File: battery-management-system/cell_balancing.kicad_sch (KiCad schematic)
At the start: 0 parts

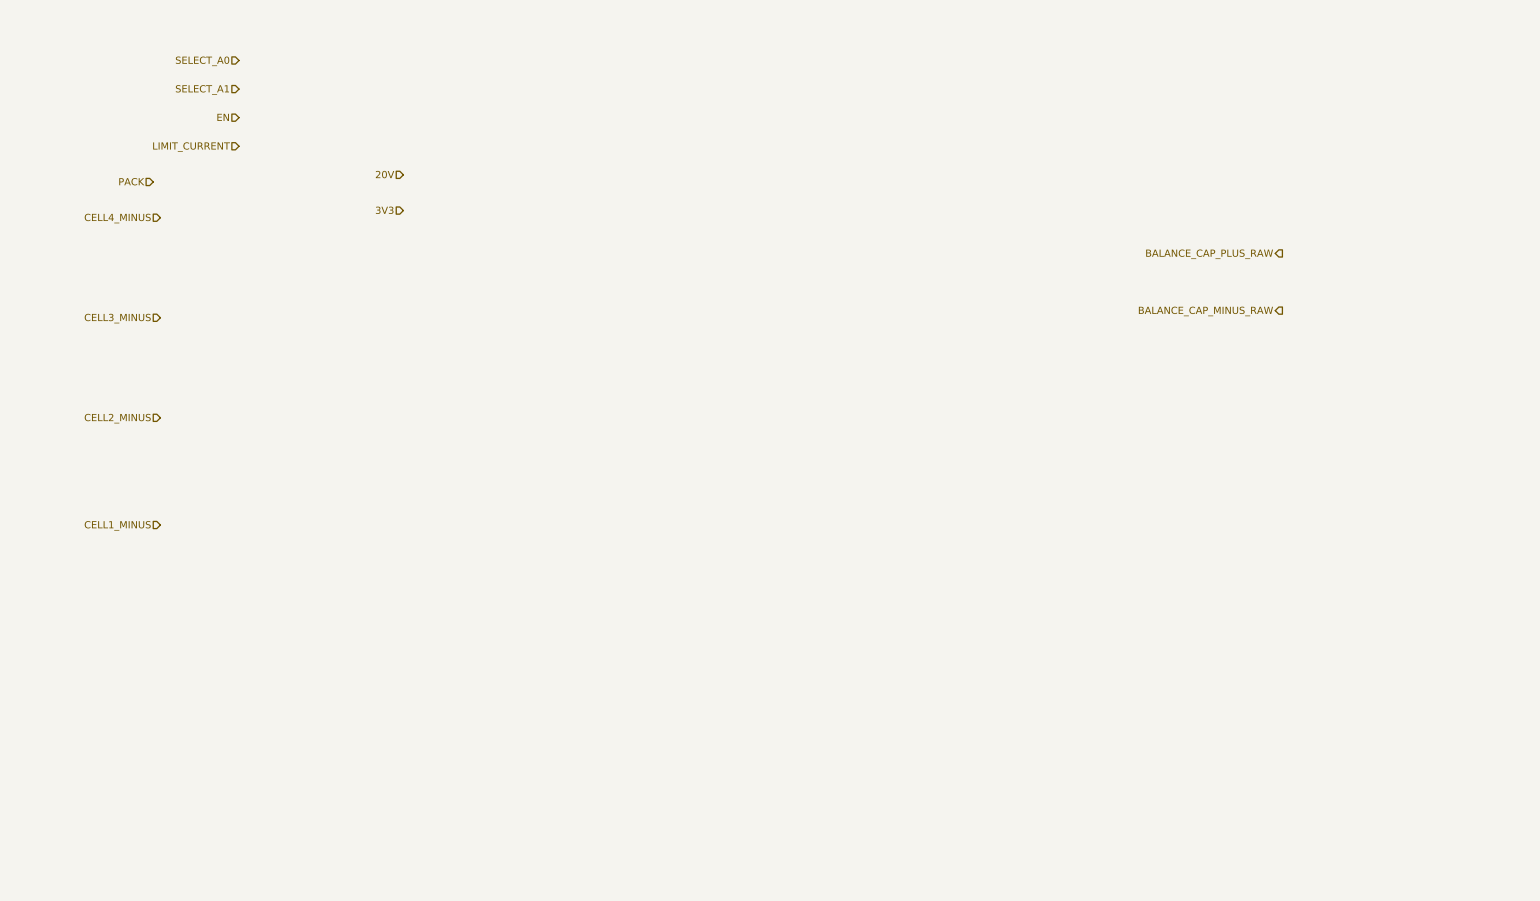
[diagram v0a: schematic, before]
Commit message: implement balancing
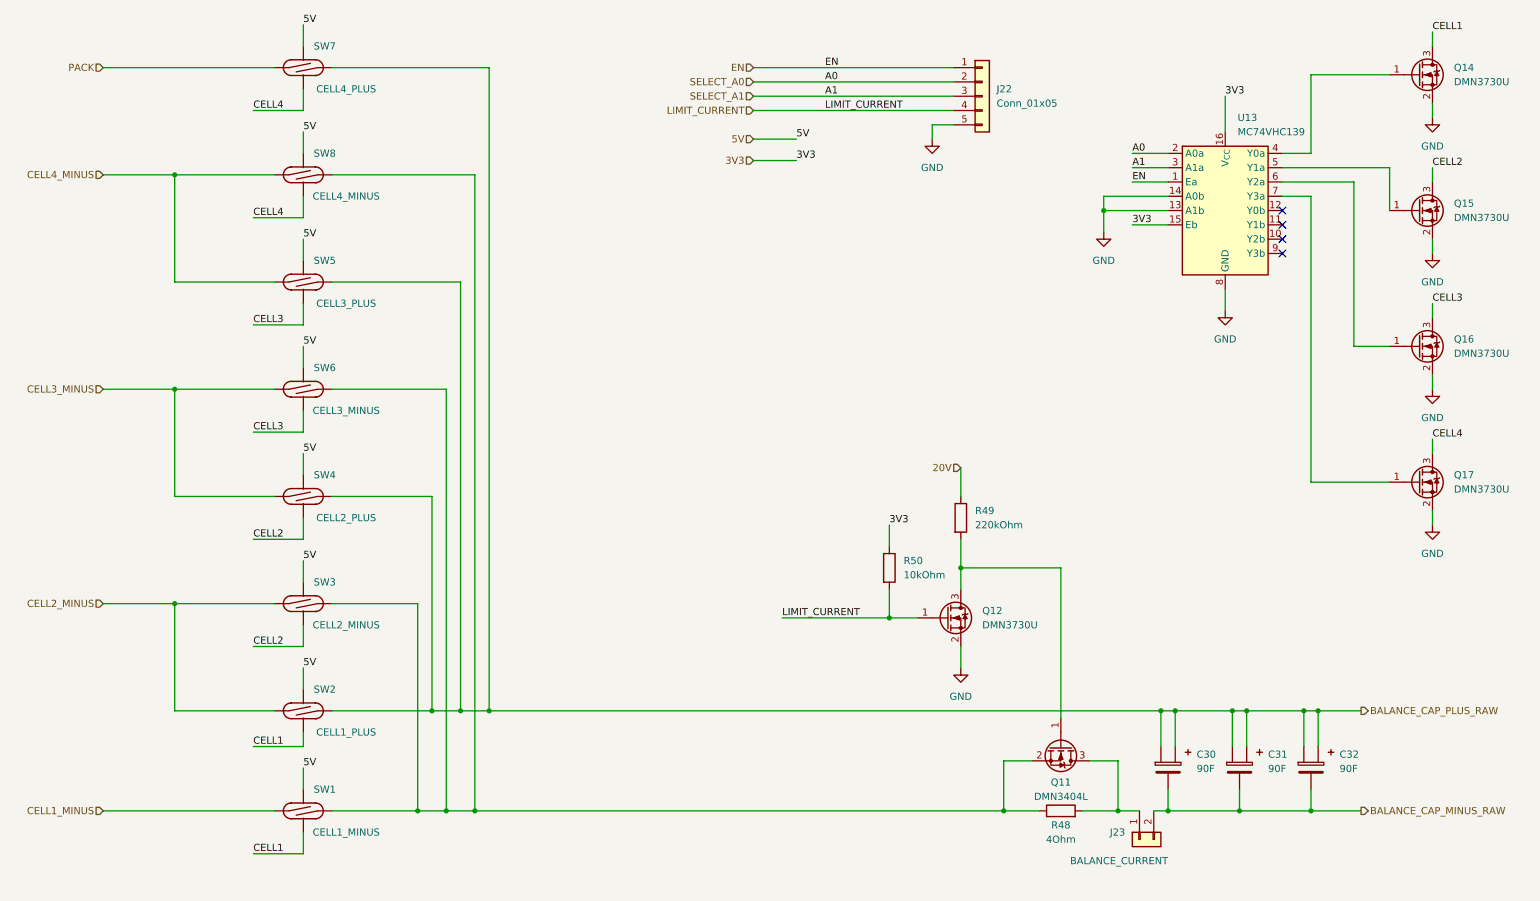
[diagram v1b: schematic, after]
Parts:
- added C30, C31, C32: 90F, benediktibk:vishay_super_cap_form_g, symbol benediktibk:C_90F_THT_4_2V
- added J22: Conn_01x05, benediktibk:PinHeader_1x05_P2.54mm_Vertical, symbol benediktibk:Conn_01x05
- added J23: BALANCE_CURRENT, benediktibk:PinHeader_1x02_P2.54mm_Vertical, symbol benediktibk:Conn_01x02
- added Q11: DMN3404L, benediktibk:SOT-23, symbol benediktibk:DMN3404L
- added Q12, Q14, Q15, Q16, Q17: DMN3730U, benediktibk:SOT-23, symbol benediktibk:DMN3730U
- added R48: 4Ohm, benediktibk:TO-263-resistor, symbol benediktibk:R_4Ohm_SMD_35W_1%
- added R49: 220kOhm, benediktibk:R_0603_1608Metric_Pad0.98x0.95mm_HandSolder, symbol benediktibk:R_220kOhm_SMD_0603_100mW_1%
- added R50: 10kOhm, benediktibk:R_0603_1608Metric_Pad0.98x0.95mm_HandSolder, symbol benediktibk:R_10kOhm_SMD_0603_100mW_1%
- added SW1: CELL1_MINUS, benediktibk:SIL05-1A72-BV669, symbol benediktibk:SIL05-1A72-BV669
- added SW2: CELL1_PLUS, benediktibk:SIL05-1A72-BV669, symbol benediktibk:SIL05-1A72-BV669
- added SW3: CELL2_MINUS, benediktibk:SIL05-1A72-BV669, symbol benediktibk:SIL05-1A72-BV669
- added SW4: CELL2_PLUS, benediktibk:SIL05-1A72-BV669, symbol benediktibk:SIL05-1A72-BV669
- added SW5: CELL3_PLUS, benediktibk:SIL05-1A72-BV669, symbol benediktibk:SIL05-1A72-BV669
- added SW6: CELL3_MINUS, benediktibk:SIL05-1A72-BV669, symbol benediktibk:SIL05-1A72-BV669
- added SW7: CELL4_PLUS, benediktibk:SIL05-1A72-BV669, symbol benediktibk:SIL05-1A72-BV669
- added SW8: CELL4_MINUS, benediktibk:SIL05-1A72-BV669, symbol benediktibk:SIL05-1A72-BV669
- added U13: MC74VHC139, benediktibk:TSSOP-16_4.4x5mm_P0.65mm, symbol benediktibk:MC74VHC139
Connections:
- net 20V: now also R49.1
- net 3V3: now also R50.1, U13.15 (Eb), U13.16 (V_{CC})
- net BALANCE_CAP_MINUS_RAW: now also C30.1, C31.1, C32.1, J23.2 (Pin_2)
- net BALANCE_CAP_PLUS_RAW: now also C30.2, C30.3, C31.2, C31.3, C32.2, C32.3, SW2.7 (+), SW4.7 (+), SW5.7 (+), SW7.7 (+)
- net CELL1_MINUS: now also SW1.1 (-)
- net CELL2_MINUS: now also SW2.1 (-), SW3.1 (-)
- net CELL3_MINUS: now also SW4.1 (-), SW6.1 (-)
- net CELL4_MINUS: now also SW5.1 (-), SW8.1 (-)
- net EN: now also J22.1 (Pin_1), U13.1 (Ea)
- net LIMIT_CURRENT: now also J22.4 (Pin_4), Q12.1 (G), R50.2
- net PACK: now also SW7.1 (-)
- net SELECT_A0: now also J22.2 (Pin_2), U13.2 (A0a)
- net SELECT_A1: now also J22.3 (Pin_3), U13.3 (A1a)
- new net: Q16.1 (G), U13.6 (Y2a)
- new net: Q14.1 (G), U13.4 (Y0a)
- new net: Q11.1 (G), Q12.3 (D), R49.2
- new net: Q11.2 (S), R48.1, SW1.7 (+), SW3.7 (+), SW6.7 (+), SW8.7 (+)
- new net: J23.1 (Pin_1), Q11.3 (D), R48.2
- new net: Q15.1 (G), U13.5 (Y1a)
- new net: Q17.1 (G), U13.7 (Y3a)
- new net 5V: SW1.2 (+), SW2.2 (+), SW3.2 (+), SW4.2 (+), SW5.2 (+), SW6.2 (+), SW7.2 (+), SW8.2 (+)
- new net CELL1: Q14.3 (D), SW1.6 (-), SW2.6 (-)
- new net CELL2: Q15.3 (D), SW3.6 (-), SW4.6 (-)
- new net CELL3: Q16.3 (D), SW5.6 (-), SW6.6 (-)
- new net CELL4: Q17.3 (D), SW7.6 (-), SW8.6 (-)
- new net GND: J22.5 (Pin_5), Q12.2 (S), Q14.2 (S), Q15.2 (S), Q16.2 (S), Q17.2 (S), U13.13 (A1b), U13.14 (A0b), U13.8 (GND)
- no-connect marks 0 -> 4

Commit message: add fuel gauge IC
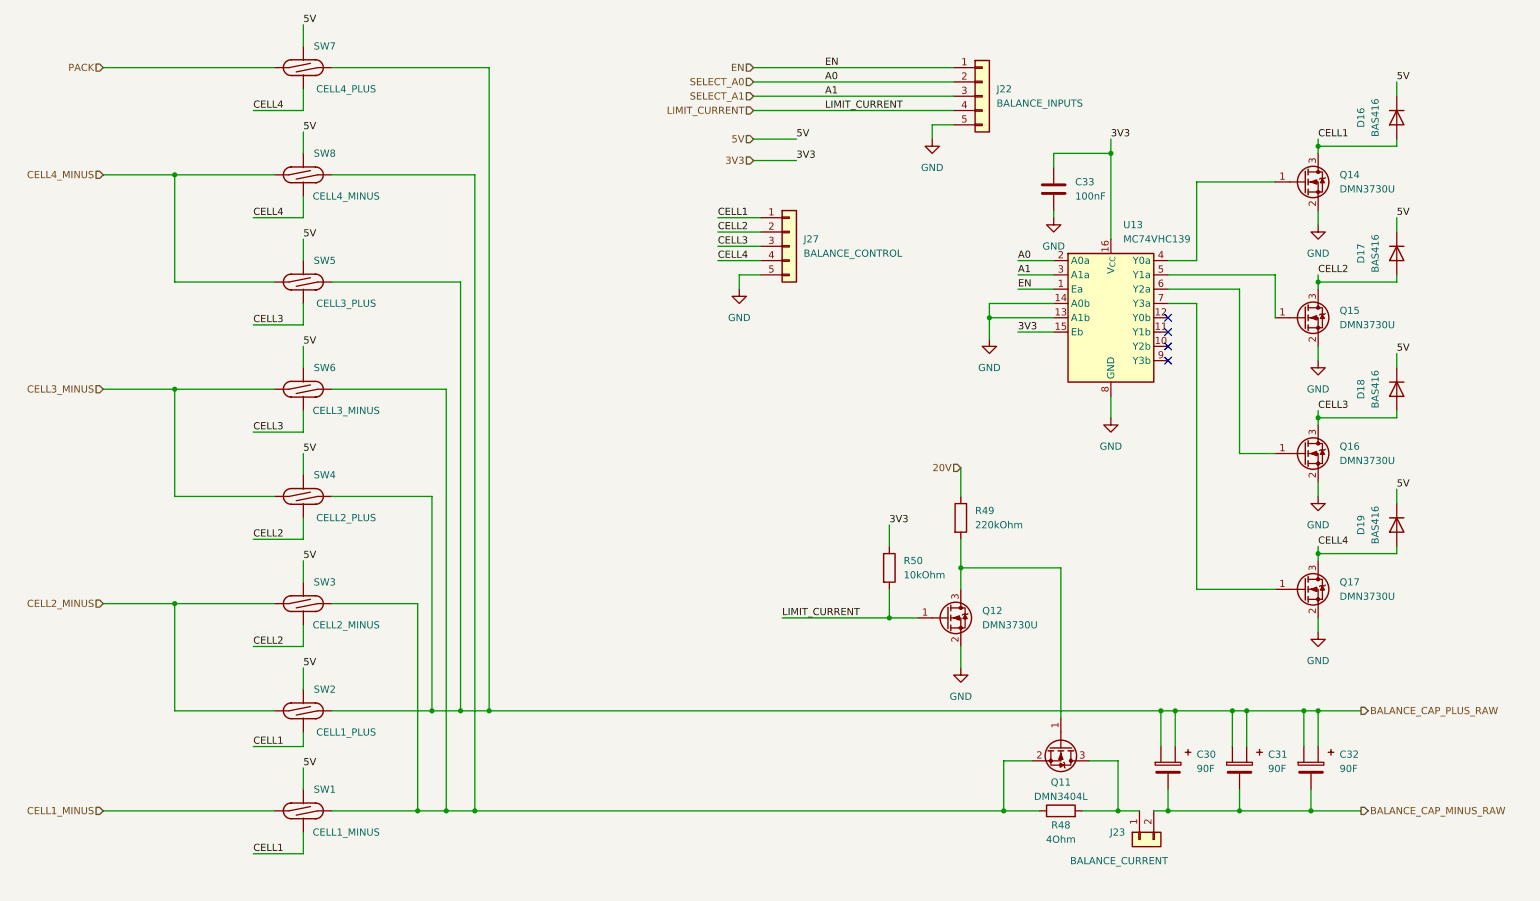
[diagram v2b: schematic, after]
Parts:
- added C33: 100nF, benediktibk:C_0603_1608Metric_Pad1.08x0.95mm_HandSolder, symbol benediktibk:C_100nF_SMD_0603_50V
- added D16, D17, D18, D19: BAS416, benediktibk:D_SOD-323, symbol benediktibk:BAS416
- added J27: BALANCE_CONTROL, benediktibk:PinHeader_1x05_P2.54mm_Vertical, symbol benediktibk:Conn_01x05
- J22: value Conn_01x05 -> BALANCE_INPUTS
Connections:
- net 3V3: now also C33.1
- net 5V: now also D16.1 (K), D17.1 (K), D18.1 (K), D19.1 (K)
- net CELL1: now also D16.2 (A), J27.1 (Pin_1)
- net CELL2: now also D17.2 (A), J27.2 (Pin_2)
- net CELL3: now also D18.2 (A), J27.3 (Pin_3)
- net CELL4: now also D19.2 (A), J27.4 (Pin_4)
- net GND: now also C33.2, J27.5 (Pin_5)
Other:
- moved on the sheet: Q14, Q15, Q16, Q17, U13

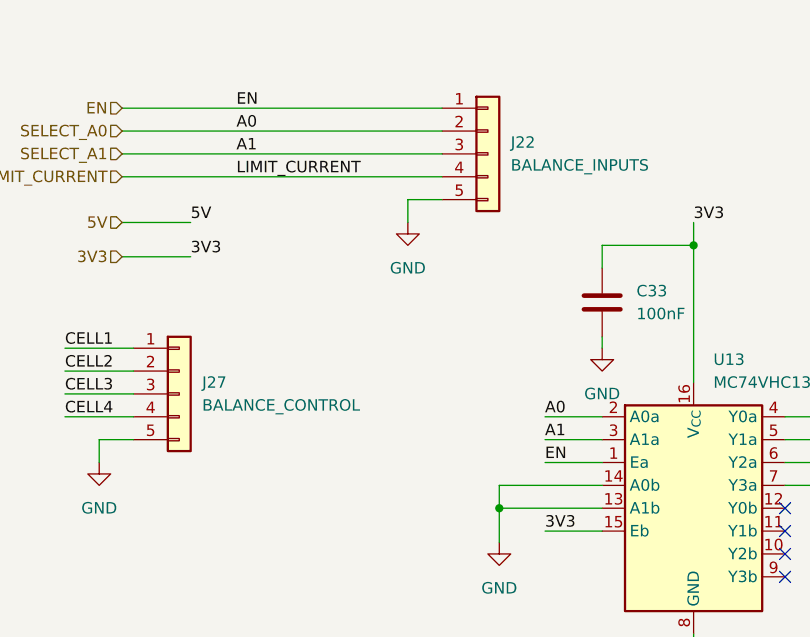
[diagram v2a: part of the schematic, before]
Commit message: fix electrical rule checker errors
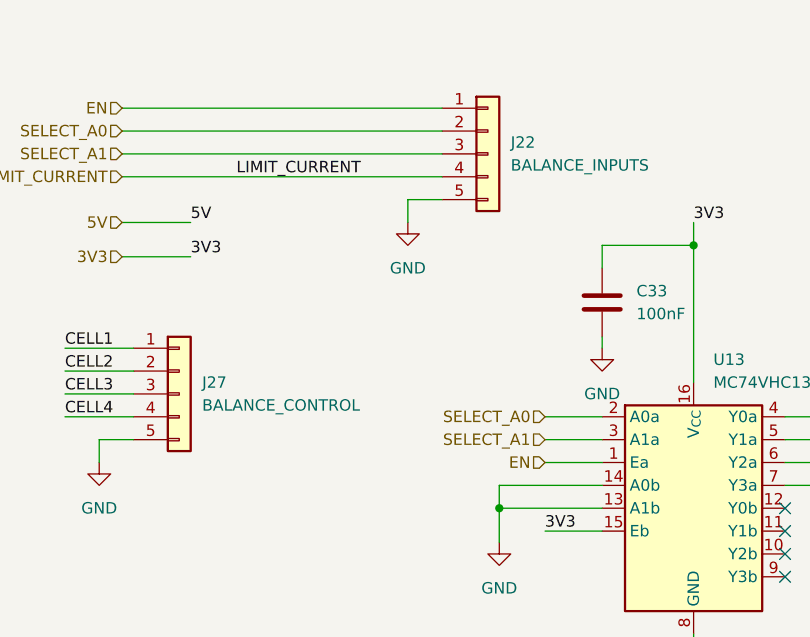
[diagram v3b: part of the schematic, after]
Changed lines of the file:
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@@
     (stroke (width 0) (type default))
-  )
-  (label "A1" (at 160.02 27.94 0) (fields_autoplaced)
-    (effects (font (size 1.27 1.27)) (justify left bottom))
-  )
-  (label "A1" (at 194.31 59.69 0) (fields_autoplaced)
-    (effects (font (size 1.27 1.27)) (justify left bottom))
   )
   (label "5V" (at 261.62 97.79 0) (fields_autoplaced)
@@
     (effects (font (size 1.27 1.27)) (justify left bottom))
   )
-  (label "A0" (at 160.02 25.4 0) (fields_autoplaced)
-    (effects (font (size 1.27 1.27)) (justify left bottom))
-  )
   (label "CELL2" (at 58.42 106.68 0) (fields_autoplaced)
     (effects (font (size 1.27 1.27)) (justify left bottom))
@@
   )
   (label "LIMIT_CURRENT" (at 160.02 30.48 0) (fields_autoplaced)
-    (effects (font (size 1.27 1.27)) (justify left bottom))
-  )
-  (label "EN" (at 160.02 22.86 0) (fields_autoplaced)
     (effects (font (size 1.27 1.27)) (justify left bottom))
   )
@@
   )
   (label "CELL3" (at 247.65 83.82 0) (fields_autoplaced)
-    (effects (font (size 1.27 1.27)) (justify left bottom))
-  )
-  (label "A0" (at 194.31 57.15 0) (fields_autoplaced)
     (effects (font (size 1.27 1.27)) (justify left bottom))
   )
@@
     (effects (font (size 1.27 1.27)) (justify left bottom))
   )
-  (label "EN" (at 194.31 62.23 0) (fields_autoplaced)
-    (effects (font (size 1.27 1.27)) (justify left bottom))
-  )
   (label "CELL3" (at 58.42 87.63 0) (fields_autoplaced)
     (effects (font (size 1.27 1.27)) (justify left bottom))
@@
     (effects (font (size 1.27 1.27)) (justify right))
   )
+  (hierarchical_label "SELECT_A0" (shape input) (at 194.31 57.15 180) (fields_autoplaced)
+    (effects (font (size 1.27 1.27)) (justify right))
+  )
   (hierarchical_label "LIMIT_CURRENT" (shape input) (at 147.32 30.48 180) (fields_autoplaced)
     (effects (font (size 1.27 1.27)) (justify right))
@@
     (effects (font (size 1.27 1.27)) (justify right))
   )
+  (hierarchical_label "EN" (shape input) (at 194.31 62.23 180) (fields_autoplaced)
+    (effects (font (size 1.27 1.27)) (justify right))
+  )
+  (hierarchical_label "SELECT_A1" (shape input) (at 194.31 59.69 180) (fields_autoplaced)
+    (effects (font (size 1.27 1.27)) (justify right))
+  )

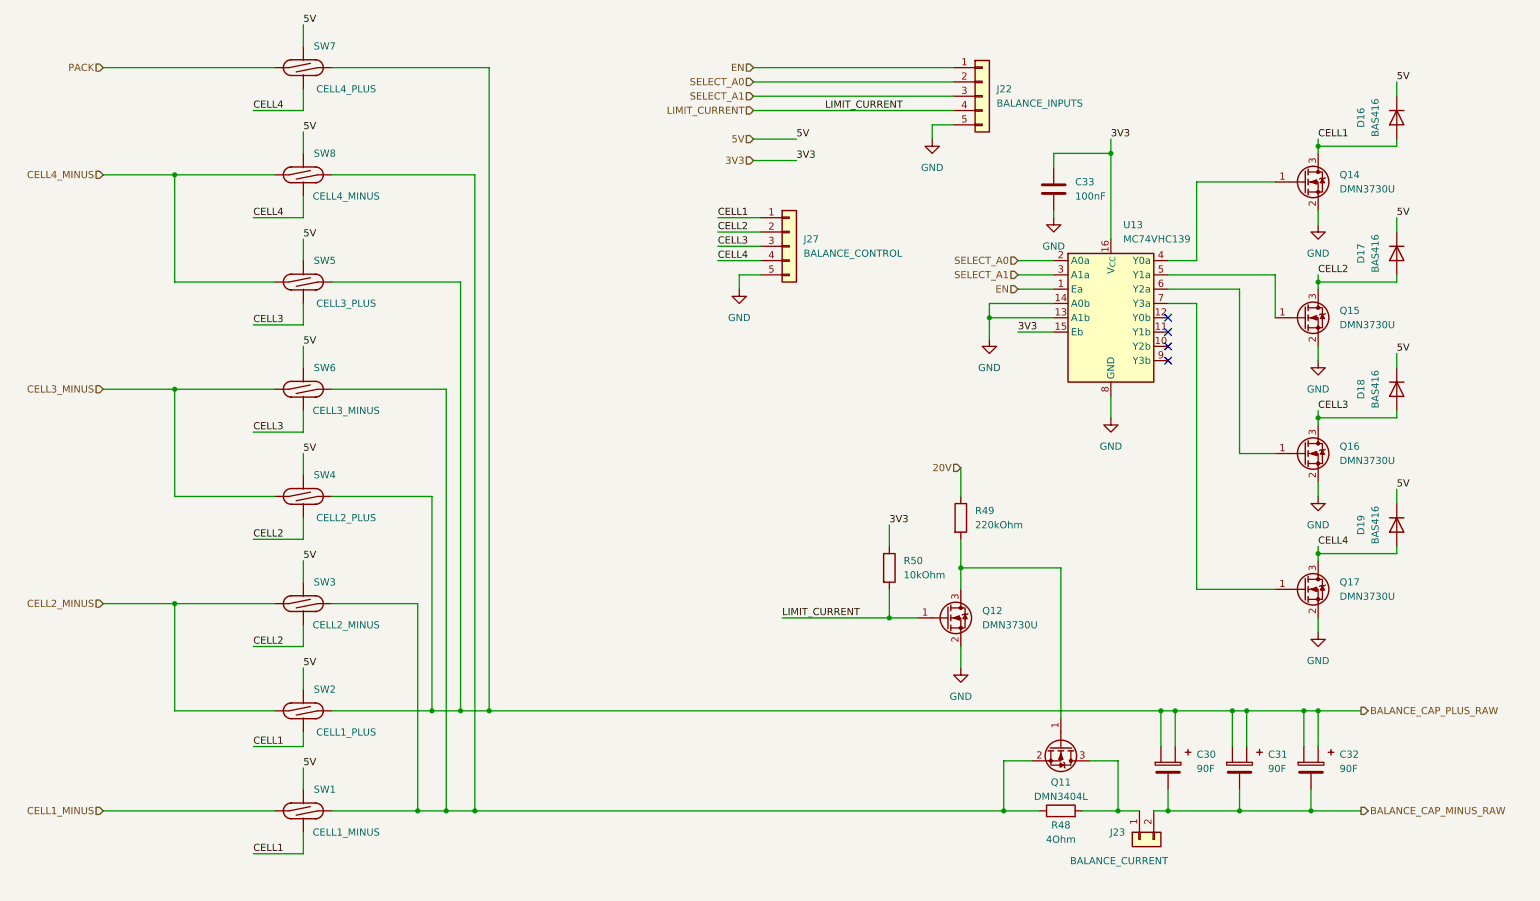
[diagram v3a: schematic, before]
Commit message: fix current sensing
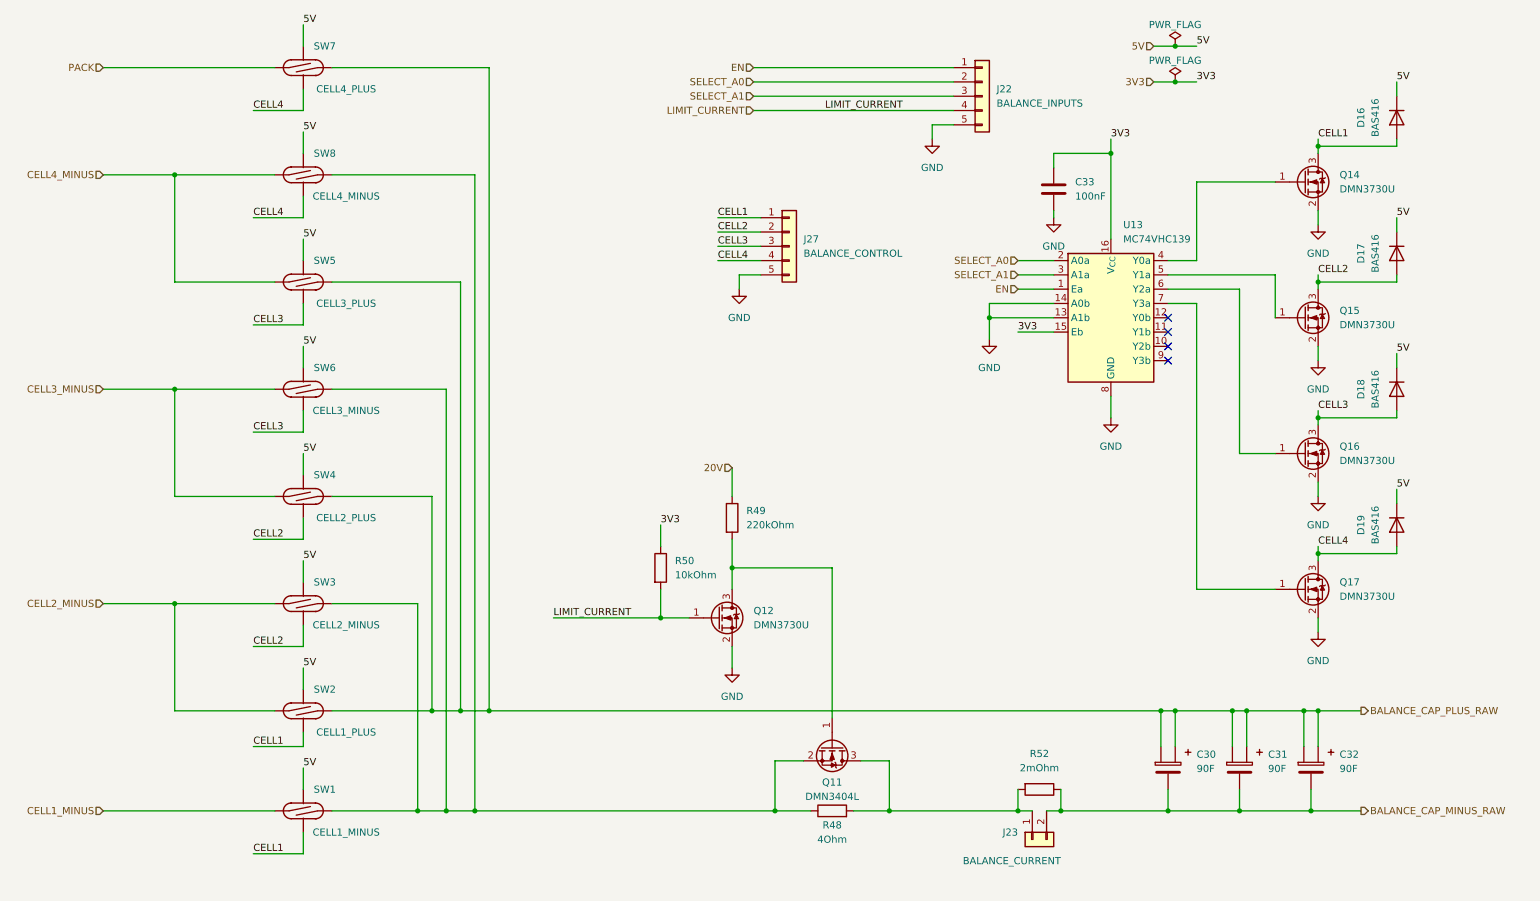
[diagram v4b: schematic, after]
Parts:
- added R52: 2mOhm, benediktibk:R_2512_6332Metric_Pad1.40x3.35mm_HandSolder, symbol benediktibk:R_2mOhm_SMD_2512_5W_1%
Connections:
- net BALANCE_CAP_MINUS_RAW: now also R52.1
- net at J23.1 (Pin_1), Q11.3 (D), R48.2: now also R52.2
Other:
- moved on the sheet: J23, Q11, Q12, R48, R49, R50
